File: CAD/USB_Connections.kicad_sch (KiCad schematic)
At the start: 14 parts, among them J8 USB_C_Plug_USB2.0, J9 USB_C_Plug_USB2.0

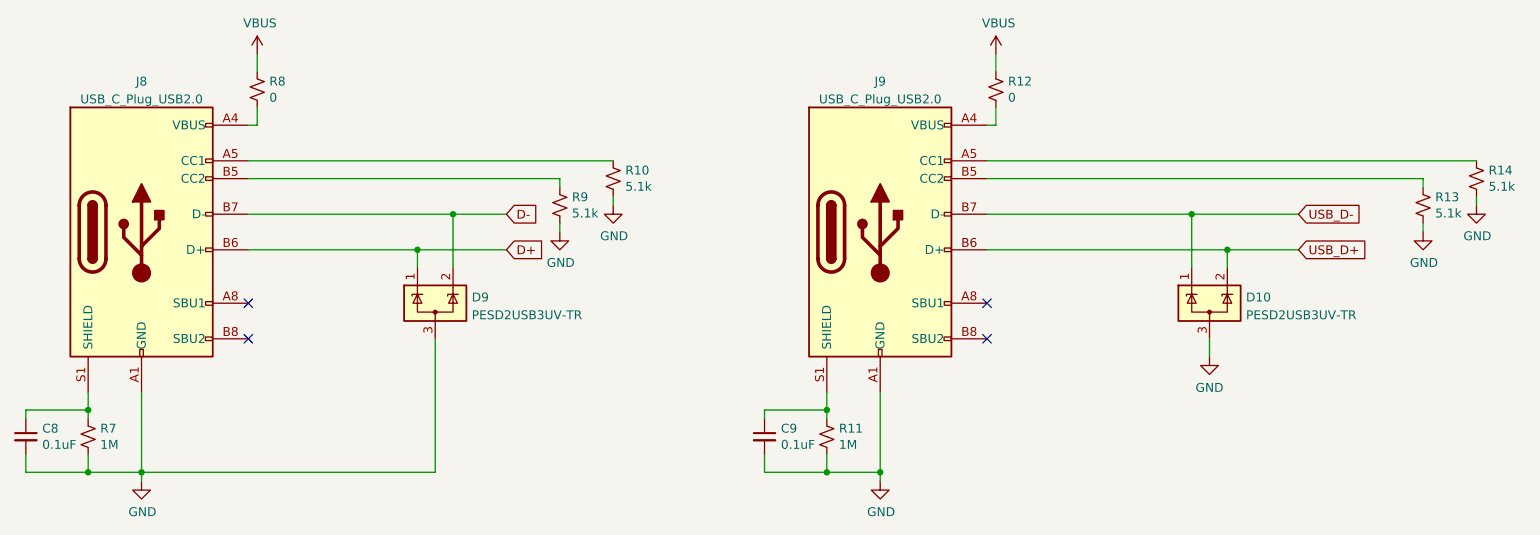
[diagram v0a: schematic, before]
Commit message: updated functional Prototype
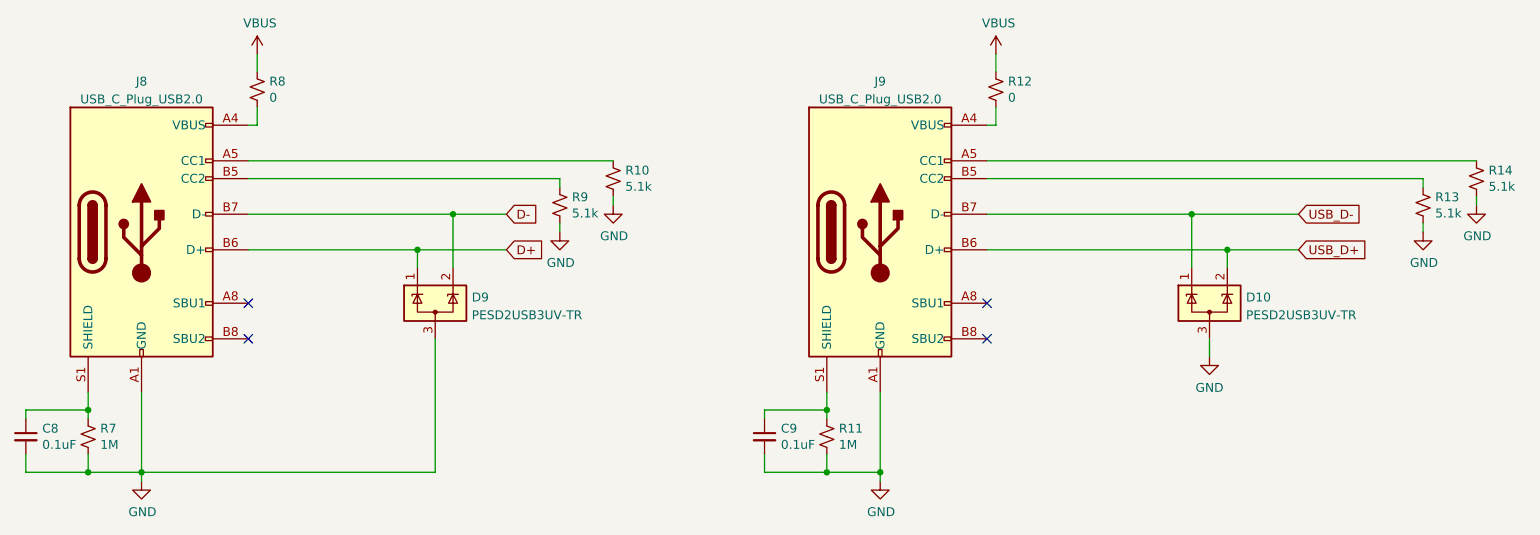
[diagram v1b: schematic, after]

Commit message: Artwork to Board and Layout
Lot o Work
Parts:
- renumbered D9 to D11, D10 to D12, J8 to J6, J9 to J7, R9 to R10, R13 to R11, R7 to R12, R11 to R13, R8 to R6, R12 to R7, R10 to R8, R14 to R9

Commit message: fine tuning
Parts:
- D11, D12: footprint Package_TO_SOT_SMD:SOT-23 -> BadgePirates:SOT-23
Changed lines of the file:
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@@
       (effects (font (size 1.27 1.27)) (justify left))
     )
-    (property "Footprint" "Package_TO_SOT_SMD:SOT-23" (at 233.045 100.33 0)
+    (property "Footprint" "BadgePirates:SOT-23" (at 233.045 100.33 0)
       (effects (font (size 1.27 1.27)) (justify left) hide)
     )
@@
       (effects (font (size 1.27 1.27)) (justify left))
     )
-    (property "Footprint" "Package_TO_SOT_SMD:SOT-23" (at 122.555 100.33 0)
+    (property "Footprint" "BadgePirates:SOT-23" (at 122.555 100.33 0)
       (effects (font (size 1.27 1.27)) (justify left) hide)
     )
